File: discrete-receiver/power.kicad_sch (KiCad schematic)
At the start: 15 parts, among them J2 Optional 5V DC Jack, U11 Ag9905LP, U12 TPS7A20xxxDBV, U13 LM66100DCK, U14 LM66100DCK, U15 LM66100DCK, U8 AMS1117

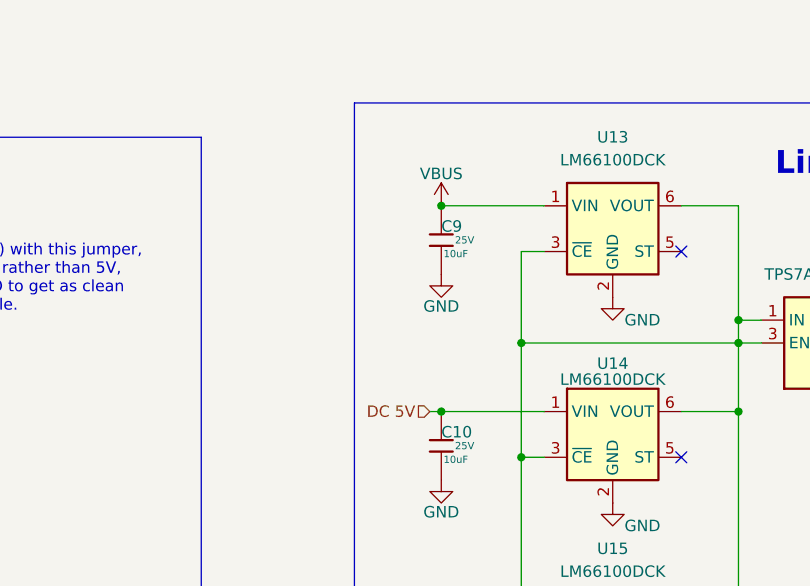
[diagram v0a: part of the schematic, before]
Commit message: Updated USB-C Symbol with JLCPCB stuff
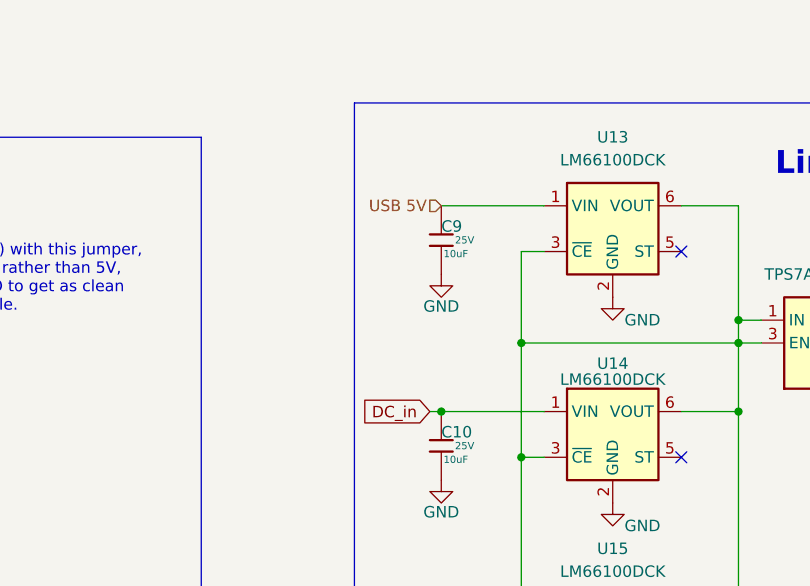
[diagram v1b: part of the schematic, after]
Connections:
- net DC 5V is gone; now on net DC_in: C10.1, U14.1 (VIN)
- net VBUS renamed USB 5V
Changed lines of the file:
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@@
-		(color 0 0 0 0)
-	)
-	(junction
-		(at 171.45 71.12)
-		(diameter 0)
 		(color 0 0 0 0)
 	)
@@
 				)
 				(justify left)
+			)
+		)
+	)
+	(global_label "DC_in"
+		(shape input)
+		(at 170.18 93.98 180)
+		(fields_autoplaced yes)
+		(effects
+			(font
+				(size 1.27 1.27)
+				(thickness 0.1588)
+			)
+			(justify right)
+		)
+		(property "Intersheetrefs" "${INTERSHEET_REFS}"
+			(at 161.9334 93.98 0)
+			(hide yes)
+			(show_name no)
+			(do_not_autoplace no)
+			(effects
+				(font
+					(size 1.27 1.27)
+				)
+				(justify right)
 			)
 		)
@@
 		)
 	)
-	(hierarchical_label "DC 5V"
+	(hierarchical_label "USB 5V"
 		(shape input)
-		(at 170.18 93.98 180)
+		(at 171.45 71.12 180)
 		(effects
 			(font
@@
 					(unit 1)
 				)
-			)
-		)
-	)
-	(symbol
-		(lib_id "power:VBUS")
-		(at 171.45 71.12 0)
-		(unit 1)
-		(body_style 1)
-		(exclude_from_sim no)
-		(in_bom yes)
-		(on_board yes)
-		(in_pos_files yes)
-		(dnp no)
-		(property "Reference" "#PWR098"
-			(at 171.45 74.93 0)
-			(hide yes)
-			(show_name no)
-			(do_not_autoplace no)
-			(effects
-				(font
-					(size 1.27 1.27)
-				)
-			)
-		)
-		(property "Value" "VBUS"
-			(at 171.45 67.564 0)
-			(show_name no)
-			(do_not_autoplace no)
-			(effects
-				(font
-					(size 1.27 1.27)
-				)
-			)
-		)
-		(property "Footprint" ""
-			(at 171.45 71.12 0)
-			(hide yes)
-			(show_name no)
-			(do_not_autoplace no)
-			(effects
-				(font
-					(size 1.27 1.27)
-				)
-			)
-		)
-		(property "Datasheet" ""
-			(at 171.45 71.12 0)
-			(hide yes)
-			(show_name no)
-			(do_not_autoplace no)
-			(effects
-				(font
-					(size 1.27 1.27)
-				)
-			)
-		)
-		(property "Description" "Power symbol creates a global label with name \"VBUS\""
-			(at 171.45 71.12 0)
-			(hide yes)
-			(show_name no)
-			(do_not_autoplace no)
-			(effects
-				(font
-					(size 1.27 1.27)
-				)
-			)
-		)
-		(pin "1"
-		)
-		(instances
-			(project "diode_tayloe_sdr"
-				(path "/d18d178d-3f10-4d68-9036-eae71a7d091a/d8c494fb-8bd9-4682-9cb3-a775cb7c5b47"
-					(reference "#PWR098")
-					(unit 1)
-				)

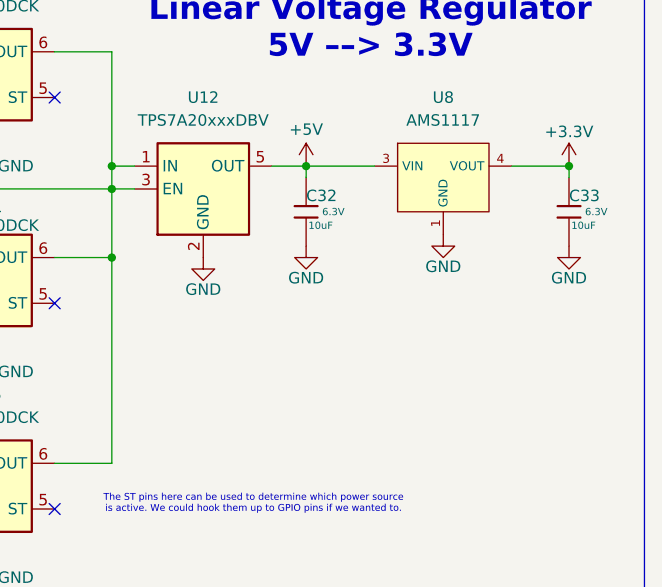
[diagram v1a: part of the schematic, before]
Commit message: Made schematic updates
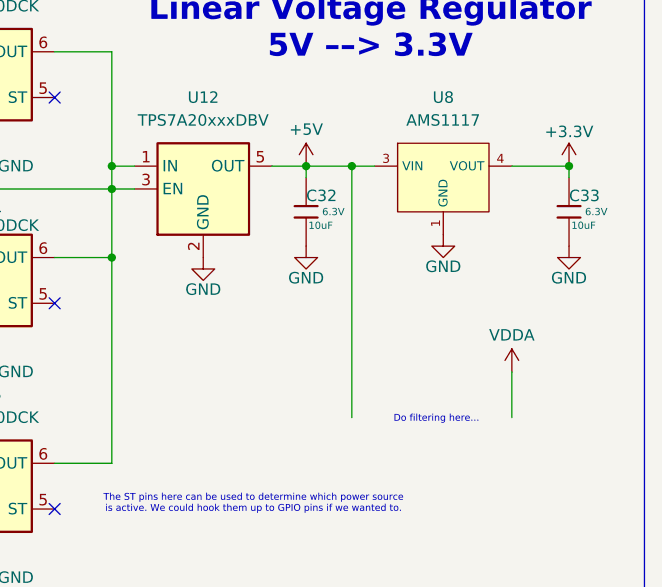
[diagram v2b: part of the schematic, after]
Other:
- note added: "Do filtering here..."
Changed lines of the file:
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@@
 		)
 	)
+	(text "Do filtering here..."
+		(exclude_from_sim no)
+		(at 240.538 112.014 0)
+		(effects
+			(font
+				(size 0.762 0.762)
+				(thickness 0.0953)
+			)
+		)
+	)
 	(text "By connecting the ADJ pin to V- (gnd) with this jumper,\nthe POE module will output 5.65V rather than 5V,\nallowing us to use a low-noise LDO to get as clean \nof a 5V rail as possible."
 		(exclude_from_sim no)
@@
 	)
 	(junction
+		(at 231.14 83.82)
+		(diameter 0)
+		(color 0 0 0 0)
+	)
+	(junction
 		(at 104.14 99.06)
 		(diameter 0)
@@
 	(wire
 		(pts
+			(xy 231.14 111.76) (xy 231.14 83.82)
+		)
+		(stroke
+			(width 0)
+			(type default)
+		)
+	)
+	(wire
+		(pts
 			(xy 40.64 109.22) (xy 40.64 87.63)
 		)
@@
 	(wire
 		(pts
+			(xy 231.14 83.82) (xy 233.68 83.82)
+		)
+		(stroke
+			(width 0)
+			(type default)
+		)
+	)
+	(wire
+		(pts
 			(xy 48.26 80.01) (xy 48.26 77.47)
 		)
@@
 	(wire
 		(pts
-			(xy 222.25 83.82) (xy 233.68 83.82)
+			(xy 222.25 83.82) (xy 231.14 83.82)
 		)
 		(stroke
@@
 	(wire
 		(pts
+			(xy 248.92 106.68) (xy 248.92 111.76)
+		)
+		(stroke
+			(width 0)
+			(type default)
+		)
+	)
+	(wire
+		(pts
 			(xy 49.53 39.37) (xy 54.61 39.37)
 		)
@@
 					(unit 1)
 				)
+			)
+		)
+	)
+	(symbol
+		(lib_id "power:+5V")
+		(at 248.92 106.68 0)
+		(unit 1)
+		(body_style 1)
+		(exclude_from_sim no)
+		(in_bom yes)
+		(on_board yes)
+		(in_pos_files yes)
+		(dnp no)
+		(property "Reference" "#PWR0119"
+			(at 248.92 110.49 0)
+			(hide yes)
+			(show_name no)
+			(do_not_autoplace no)
+			(effects
+				(font
+					(size 1.27 1.27)
+				)
+			)
+		)
+		(property "Value" "VDDA"
+			(at 248.92 102.616 0)
+			(show_name no)
+			(do_not_autoplace no)
+			(effects
+				(font
+					(size 1.27 1.27)
+				)
+			)
+		)
+		(property "Footprint" ""
+			(at 248.92 106.68 0)
+			(hide yes)
+			(show_name no)
+			(do_not_autoplace no)
+			(effects
+				(font
+					(size 1.27 1.27)
+				)
+			)
+		)
+		(property "Datasheet" ""
+			(at 248.92 106.68 0)
+			(hide yes)
+			(show_name no)
+			(do_not_autoplace no)
+			(effects
+				(font
+					(size 1.27 1.27)
+				)
+			)
+		)
+		(property "Description" "Power symbol creates a global label with name \"+5V\""
+			(at 248.92 106.68 0)
+			(hide yes)
+			(show_name no)
+			(do_not_autoplace no)
+			(effects
+				(font
+					(size 1.27 1.27)
+				)
+			)
+		)
+		(pin "1"
+		)
+		(instances
+			(project "diode_tayloe_sdr"
+				(path "/d18d178d-3f10-4d68-9036-eae71a7d091a/d8c494fb-8bd9-4682-9cb3-a775cb7c5b47"
+					(reference "#PWR0119")
+					(unit 1)
+				)

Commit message: Updated schematic
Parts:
- added C67: 10uF, PCM_JLCPCB:C_0402, symbol PCM_JLCPCB-Capacitors:0402,10uF
- added FB3: FB, symbol Device:FerriteBead_Small
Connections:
- net +5V: now also FB3.1
- net GND: now also C67.2
- net VDDA: now also C67.1, FB3.2

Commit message: :)
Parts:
- removed C32, C33, C67: 10uF, PCM_JLCPCB:C_0402, symbol PCM_JLCPCB-Capacitors:0402,10uF
- added C32: 100pF, PCM_JLCPCB:C_0603, symbol PCM_JLCPCB-Capacitors:0603,100pF
- added C34, C60, C67: 10uF, PCM_JLCPCB:C_0603, symbol PCM_JLCPCB-Capacitors:0603,10uF,(2)
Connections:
- net +3.3V: now also C67.1
- net +5V: now also C60.1
- net GND: now also C32.2, C34.2, C60.2, C67.2
- net VDDA: now also C32.1, C34.1
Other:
- moved on the sheet: FB3

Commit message: :)
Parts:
- C10, C11, C9: Manufacturer Samsung Electro-Mechanics -> (none); Price 0.021USD -> (none)
- C32: Manufacturer Samsung Electro-Mechanics -> (none); Price 0.007USD -> (none)
- C34, C60, C67: Manufacturer Samsung Electro-Mechanics -> (none); Price 0.020USD -> (none)
- U8: Manufacturer Advanced Monolithic Systems -> (none); Price 0.169USD -> (none)
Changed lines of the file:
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@@
 			)
 		)
-		(property "Price" "0.021USD"
-			(at 171.45 97.79 0)
-			(hide yes)
-			(show_name no)
-			(do_not_autoplace no)
-			(effects
-				(font
-					(size 1.27 1.27)
-				)
-			)
-		)
 		(property "Process" "SMT"
 			(at 171.45 97.79 0)
@@
 			)
 		)
-		(property "Manufacturer" "Samsung Electro-Mechanics"
-			(at 171.45 97.79 0)
-			(hide yes)
-			(show_name no)
-			(do_not_autoplace no)
-			(effects
-				(font
-					(size 1.27 1.27)
-				)
-			)
-		)
 		(property "Part" "CL10A106MA8NRNC"
 			(at 171.45 97.79 0)
@@
 			)
 		)
-		(property "Price" "0.169USD"
-			(at 241.3 86.36 0)
-			(hide yes)
-			(show_name no)
-			(do_not_autoplace no)
-			(effects
-				(font
-					(size 1.27 1.27)
-				)
-			)
-		)
 		(property "Process" "SMT"
 			(at 241.3 86.36 0)
@@
 			)
 		)
-		(property "Manufacturer" "Advanced Monolithic Systems"
-			(at 241.3 86.36 0)
-			(hide yes)
-			(show_name no)
-			(do_not_autoplace no)
-			(effects
-				(font
-					(size 1.27 1.27)
-				)
-			)
-		)
 		(property "Part" "AMS1117-3.3"
 			(at 241.3 86.36 0)
@@
 			)
 		)
-		(property "Price" "0.020USD"
-			(at 223.52 88.9 0)
-			(hide yes)
-			(show_name no)
-			(do_not_autoplace no)
-			(effects
-				(font
-					(size 1.27 1.27)
-				)
-			)
-		)
 		(property "Process" "SMT"
 			(at 223.52 88.9 0)
@@
 			)
 		)
-		(property "Manufacturer" "Samsung Electro-Mechanics"
-			(at 223.52 88.9 0)
-			(hide yes)
-			(show_name no)
-			(do_not_autoplace no)
-			(effects
-				(font
-					(size 1.27 1.27)
-				)
-			)
-		)
 		(property "Part" "CL10A106MA8NRNC"
 			(at 223.52 88.9 0)
@@
 			)
 		)
-		(property "Price" "0.021USD"
-			(at 175.26 120.65 0)
-			(hide yes)
-			(show_name no)
-			(do_not_autoplace no)
-			(effects
-				(font
-					(size 1.27 1.27)
-				)
-			)
-		)
 		(property "Process" "SMT"
 			(at 175.26 120.65 0)
@@
 			)
 		)
-		(property "Manufacturer" "Samsung Electro-Mechanics"
-			(at 175.26 120.65 0)
-			(hide yes)
-			(show_name no)
-			(do_not_autoplace no)
-			(effects
-				(font
-					(size 1.27 1.27)
-				)
-			)
-		)
 		(property "Part" "CL10A106MA8NRNC"
 			(at 175.26 120.65 0)
@@
 			)
 		)
-		(property "Price" "0.020USD"
-			(at 255.27 88.9 0)
-			(hide yes)
-			(show_name no)
-			(do_not_autoplace no)
-			(effects
-				(font
-					(size 1.27 1.27)
-				)
-			)
-		)
 		(property "Process" "SMT"
 			(at 255.27 88.9 0)
@@
 			)
 		)
-		(property "Manufacturer" "Samsung Electro-Mechanics"
-			(at 255.27 88.9 0)
-			(hide yes)
-			(show_name no)
-			(do_not_autoplace no)
-			(effects
-				(font
-					(size 1.27 1.27)
-				)
-			)
-		)
 		(property "Part" "CL10A106MA8NRNC"
 			(at 255.27 88.9 0)
@@
 			)
 		)
-		(property "Price" "0.021USD"
-			(at 171.45 74.93 0)
-			(hide yes)
-			(show_name no)
-			(do_not_autoplace no)
-			(effects
-				(font
-					(size 1.27 1.27)
-				)
-			)
-		)
 		(property "Process" "SMT"
 			(at 171.45 74.93 0)
@@
 			)
 		)
-		(property "Manufacturer" "Samsung Electro-Mechanics"
-			(at 171.45 74.93 0)
-			(hide yes)
-			(show_name no)
-			(do_not_autoplace no)
-			(effects
-				(font
-					(size 1.27 1.27)
-				)
-			)
-		)
 		(property "Part" "CL10A106MA8NRNC"
 			(at 171.45 74.93 0)
@@
 			)
 		)
-		(property "Price" "0.007USD"
-			(at 232.41 110.49 0)
-			(hide yes)
-			(show_name no)
-			(do_not_autoplace no)
-			(effects
-				(font
-					(size 1.27 1.27)
-				)
-			)
-		)
 		(property "Process" "SMT"
 			(at 232.41 110.49 0)
@@
 			)
 		)
-		(property "Manufacturer" "Samsung Electro-Mechanics"
-			(at 232.41 110.49 0)
-			(hide yes)
-			(show_name no)
-			(do_not_autoplace no)
-			(effects
-				(font
-					(size 1.27 1.27)
-				)
-			)
-		)
 		(property "Part" "CL10C101JB8NNNC"
 			(at 232.41 110.49 0)
@@
 			)
 		)
-		(property "Price" "0.020USD"
-			(at 250.19 110.49 0)
-			(hide yes)
-			(show_name no)
-			(do_not_autoplace no)
-			(effects
-				(font
-					(size 1.27 1.27)
-				)
-			)
-		)
 		(property "Process" "SMT"
 			(at 250.19 110.49 0)
@@
 			(at 250.19 110.49 0)
 			(hide yes)
-			(show_name no)
-			(do_not_autoplace no)
-			(effects
-				(font
-					(size 1.27 1.27)
-				)
-			)
-		)
-		(property "Manufacturer" "Samsung Electro-Mechanics"
-			(at 250.19 110.49 0)
-			(hide yes)

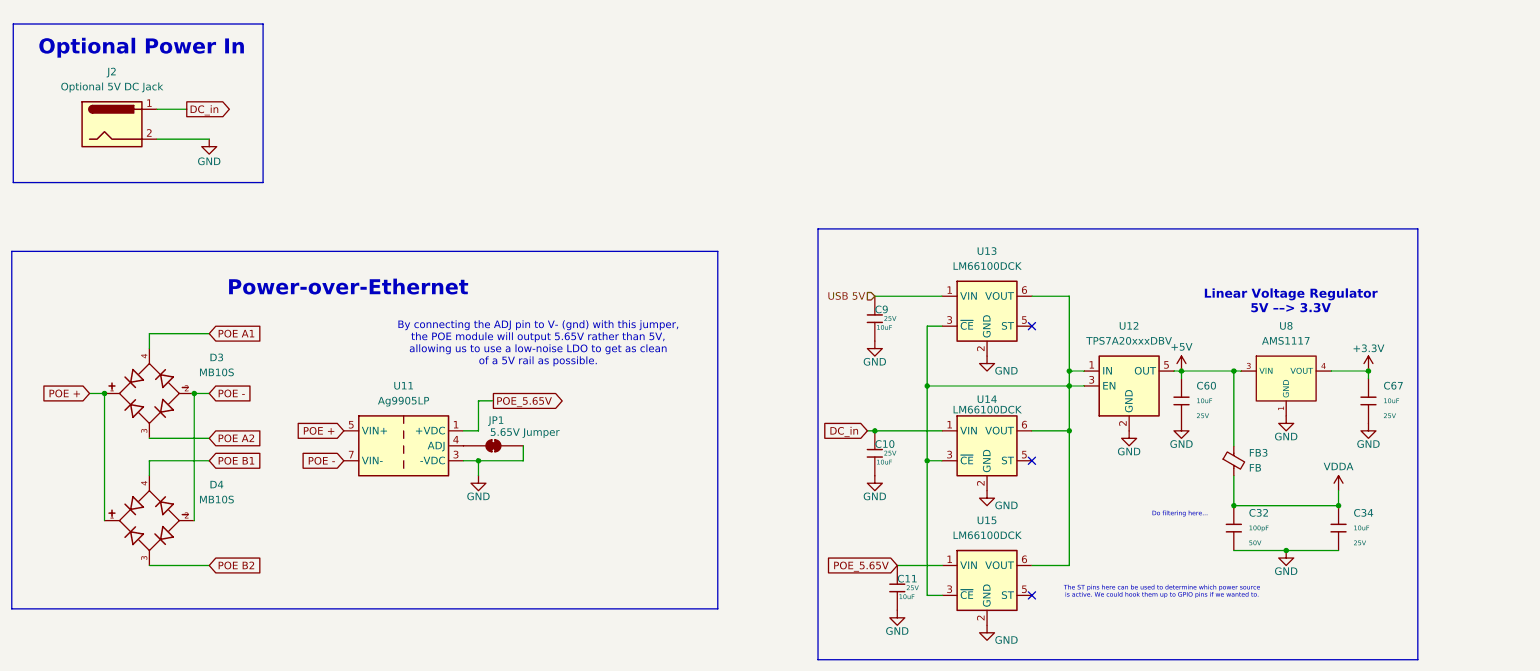
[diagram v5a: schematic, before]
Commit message: power test points and jumpers
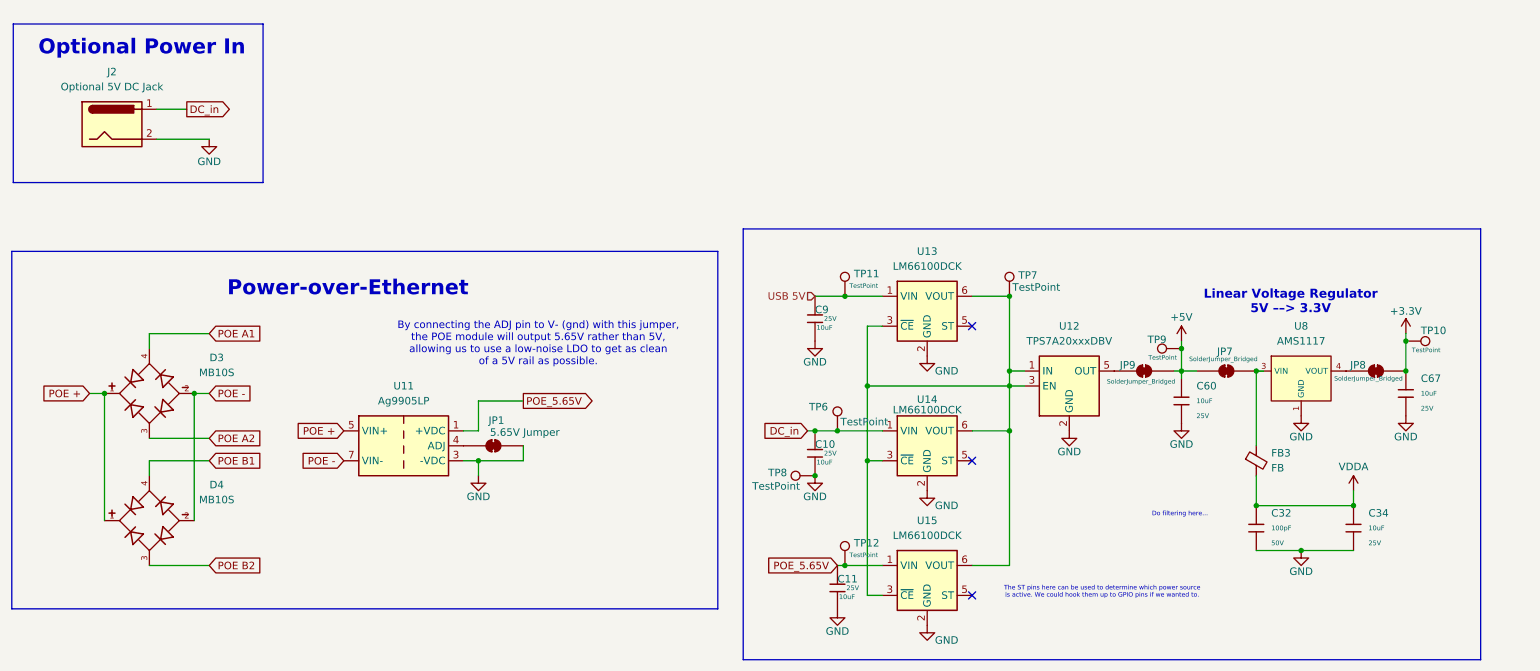
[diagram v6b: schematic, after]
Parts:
- added JP7, JP8, JP9: SolderJumper_Bridged, symbol Jumper:SolderJumper_2_Bridged
- added TP10, TP11, TP12, TP6, TP7, TP8, TP9: TestPoint, symbol Connector:TestPoint
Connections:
- net +3.3V: now also JP8.2 (B), TP10.1; no longer U8.2 (VOUT), U8.4 (VOUT)
- net +5V: now also JP7.1 (A), JP9.2 (B), TP9.1; no longer FB3.1, U12.5 (OUT), U8.3 (VIN)
- net DC_in: now also TP6.1
- net GND: now also TP8.1
- net POE_5.65V: now also TP12.1
- net USB 5V: now also TP11.1
- net at U12.1 (IN), U12.3 (EN), U13.3 (~{CE})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: now also TP7.1
- new net: JP8.1 (A), U8.2 (VOUT), U8.4 (VOUT)
- new net: FB3.1, JP7.2 (B), U8.3 (VIN)
- new net: JP9.1 (A), U12.5 (OUT)
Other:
- moved on the sheet: C10, C11, C32, C34, C67, C9, FB3, U12, U13, U14, U15, U8

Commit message: Progress made on schematic
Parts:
- added C33, C55: 100nF, PCM_JLCPCB:C_0402, symbol PCM_JLCPCB-Capacitors:0402,100nF
- added C70: 100pF, PCM_JLCPCB:C_0603, symbol PCM_JLCPCB-Capacitors:0603,100pF
- added TP13: VDDA, symbol Connector:TestPoint
- J2: footprint (none) -> sdr_project:CUI_PJ-102BH
- TP10: value TestPoint -> +3.3V
- TP11: value TestPoint -> USB_IN
- TP12: value TestPoint -> POE_IN
- TP6: value TestPoint -> DC_IN
- TP7: value TestPoint -> VIN
- TP8: value TestPoint -> GND
- TP9: value TestPoint -> +5V
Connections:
- net +5V: now also FB3.2, C55.1, C70.1
- net GND: now also C33.2, C55.2, C70.2
- net VDDA: now also FB3.1, C33.1, TP13.1; no longer FB3.2
- net at JP7.2 (B), U8.3 (VIN): no longer FB3.1
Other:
- note removed: "Do filtering here..."
- moved on the sheet: C32, C34, C60

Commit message: Started to redo power
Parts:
- removed JP9: SolderJumper_Bridged, symbol Jumper:SolderJumper_2_Bridged
- added U20: (no value), EasyEDA_Lib:TDFN-8_L3.0-W3.0-P0.65-BL-EP2.3, symbol EasyEDA_Lib:HX59800-SQ
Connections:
- net +5V: now also TP7.1, U13.3 (~{CE}), U13.6 (VOUT), U14.3 (~{CE}), U14.6 (VOUT), U15.3 (~{CE}), U15.6 (VOUT); no longer FB3.2
- net GND: no longer U12.2 (GND)
- net VDDA renamed +5V_A
- now unconnected: U12.1 (IN), U12.3 (EN)
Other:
- note added: "3.3V LDO Regulator"
- note added: "Old Voltage Regulator"
- note removed: "Linear Voltage Regulator 5V ––> 3.3V"
- moved on the sheet: C67, JP7, JP8, TP10, U8
